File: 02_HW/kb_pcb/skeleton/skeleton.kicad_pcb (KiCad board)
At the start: 2 copper layers, 65 parts, among them J1 Adafruit_Feather_16_pin, J2 Adafruit_feather_12_pin, SW1 SW_Push, SW10 SW_Push, SW11 SW_Push, SW12 SW_Push, SW13 SW_Push, SW14 SW_Push, SW15 SW_Push, SW16 SW_Push, SW17 SW_Push, SW18 SW_Push, SW19 SW_Push, SW2 SW_Push, SW20 SW_Push, SW21 SW_Push, SW22 SW_Push, SW23 SW_Push, SW24 SW_Push, SW25 SW_Push, SW26 SW_Push, SW27 SW_Push, SW28 SW_Push, SW29 SW_Push, SW3 SW_Push, SW30 SW_Push, SW4 SW_Push, SW6 SW_Push, SW7 SW_Push, SW8 SW_Push, SW9 SW_Push

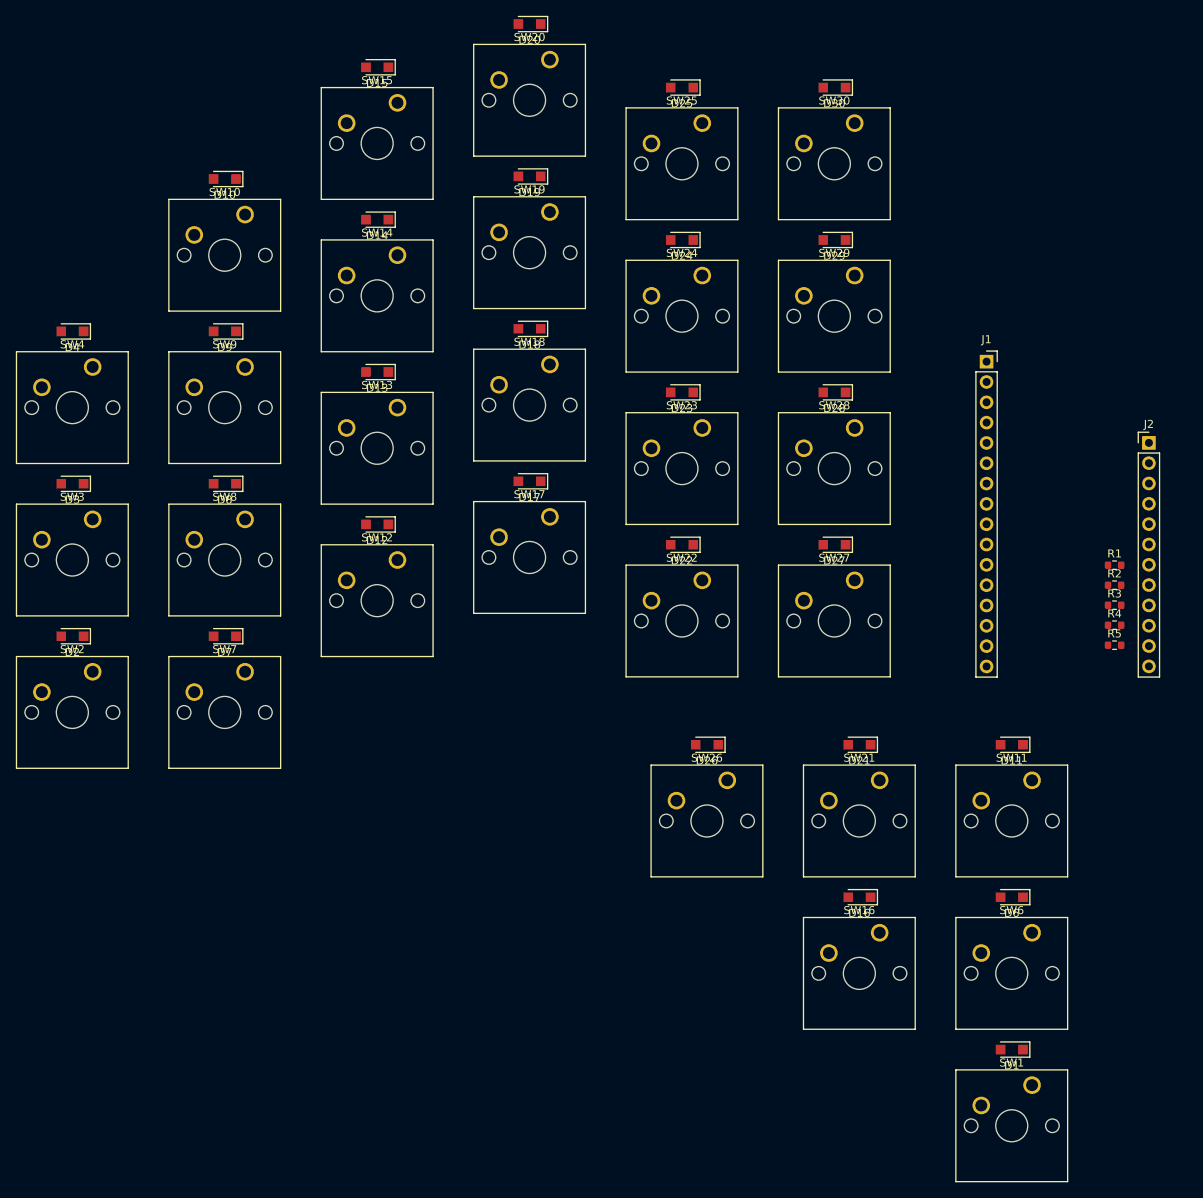
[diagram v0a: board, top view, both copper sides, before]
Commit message: Updated thumb pad layout, rearranged silkscreen
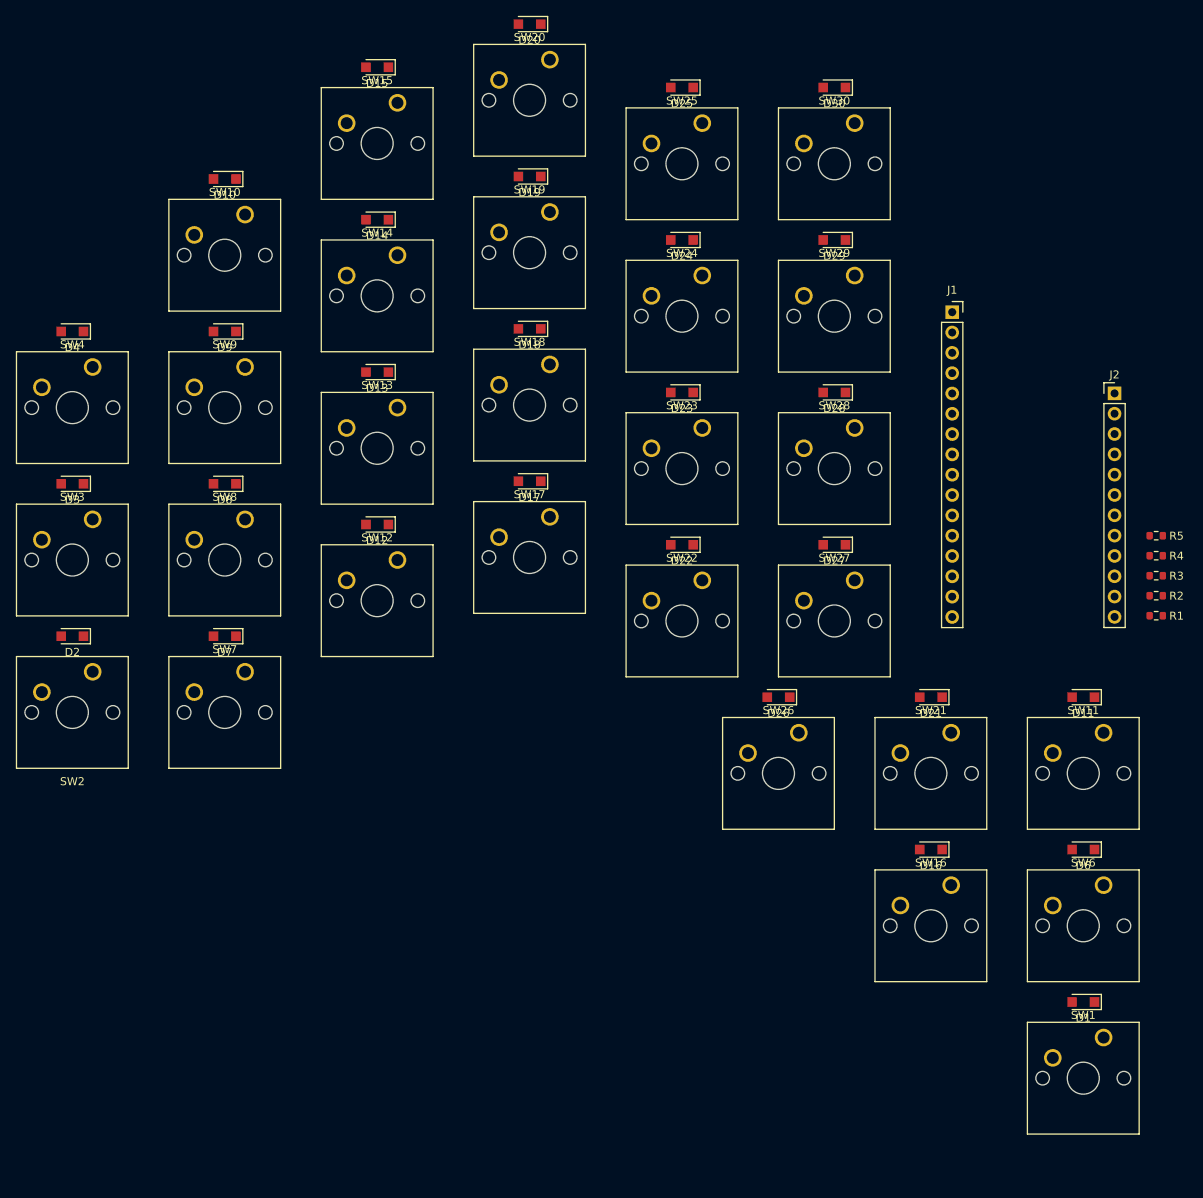
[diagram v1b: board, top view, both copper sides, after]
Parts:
- moved R5 14.6 mm to (165.7, 99.8), turned to 180 degrees
- moved SW21 10.7 mm to (140.1, 124.4)
- moved SW16 10.7 mm to (140.1, 143.5)
- moved D1 10.7 mm to (156.6, 158.1)
- moved SW1 10.7 mm to (159.1, 162.5)
- moved SW11 10.7 mm to (159.1, 124.4)
- moved SW26 10.7 mm to (121.0, 124.4)
- moved D11 10.7 mm to (156.6, 120.0)
- moved D21 10.7 mm to (137.5, 120.0)
- moved D26 10.7 mm to (118.5, 120.0)
- moved D16 10.7 mm to (137.5, 139.1)
- moved D6 10.7 mm to (156.6, 139.1)
- moved SW6 10.7 mm to (159.1, 143.5)
- moved R4 10.1 mm to (165.7, 102.3), turned to 180 degrees
- moved R1 8.18 mm to (165.7, 109.8), turned to 180 degrees
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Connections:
- J1 pad 10: unconnected-(J1-Pin_10-Pad10) -> /Col_4
- J1 pad 11: unconnected-(J1-Pin_11-Pad11) -> /Col_5
- J1 pad 6: unconnected-(J1-Pin_6-Pad6) -> /Col_0
- J1 pad 7: unconnected-(J1-Pin_7-Pad7) -> /Col_1
- J1 pad 8: unconnected-(J1-Pin_8-Pad8) -> /Col_2
- J1 pad 9: unconnected-(J1-Pin_9-Pad9) -> /Col_3
- J2 pad 1: /Col_0 -> unconnected-(J2-Pin_1-Pad1)
- J2 pad 10: /Row_3 -> /Row_2
- J2 pad 11: /Row_4 -> /Row_1
- J2 pad 12: unconnected-(J2-Pin_12-Pad12) -> /Row_0
- J2 pad 2: /Col_1 -> unconnected-(J2-Pin_2-Pad2)
- J2 pad 3: /Col_2 -> unconnected-(J2-Pin_3-Pad3)
- J2 pad 4: /Col_3 -> unconnected-(J2-Pin_4-Pad4)
- J2 pad 5: /Col_4 -> unconnected-(J2-Pin_5-Pad5)
- J2 pad 6: /Col_5 -> unconnected-(J2-Pin_6-Pad6)
- J2 pad 7: /Row_0 -> unconnected-(J2-Pin_7-Pad7)
- J2 pad 8: /Row_1 -> /Row_4
- J2 pad 9: /Row_2 -> /Row_3
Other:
- rule pad_to_mask_clearance: 0 -> 0.038
